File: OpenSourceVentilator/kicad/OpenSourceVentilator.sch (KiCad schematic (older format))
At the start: 7 parts, among them J101 Conn_TM1638_Disp, J102 12V Barrel Jack, J103 Conn_Stepper_Motor, U101 BME280

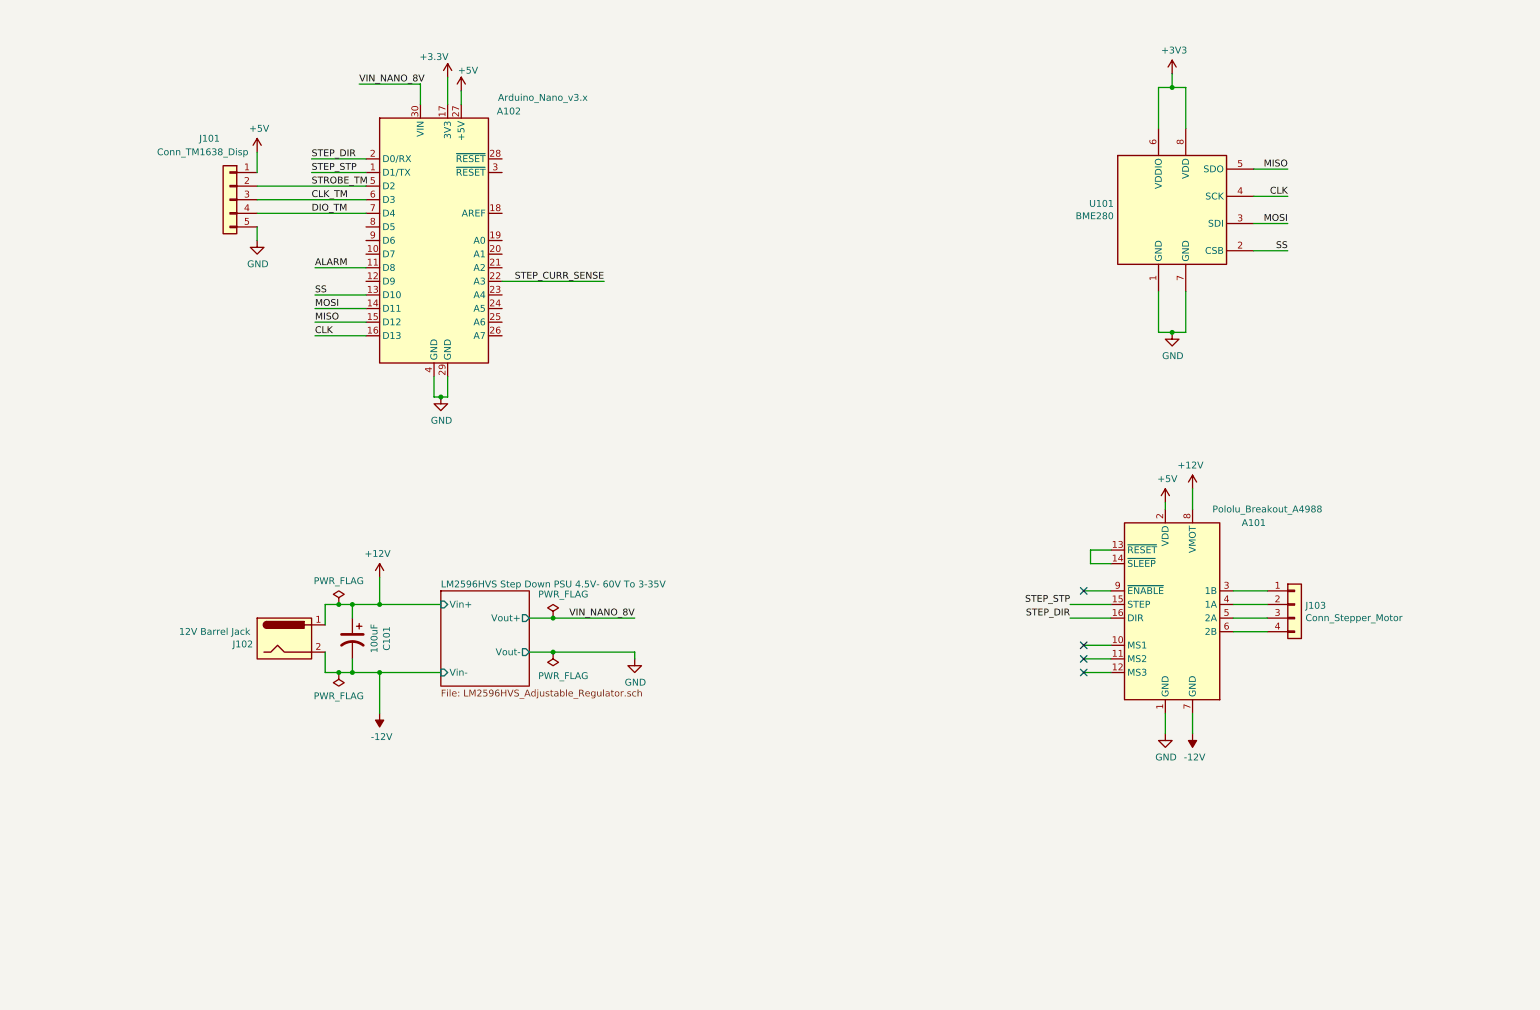
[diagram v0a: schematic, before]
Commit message: Initial schematic draft for OSV
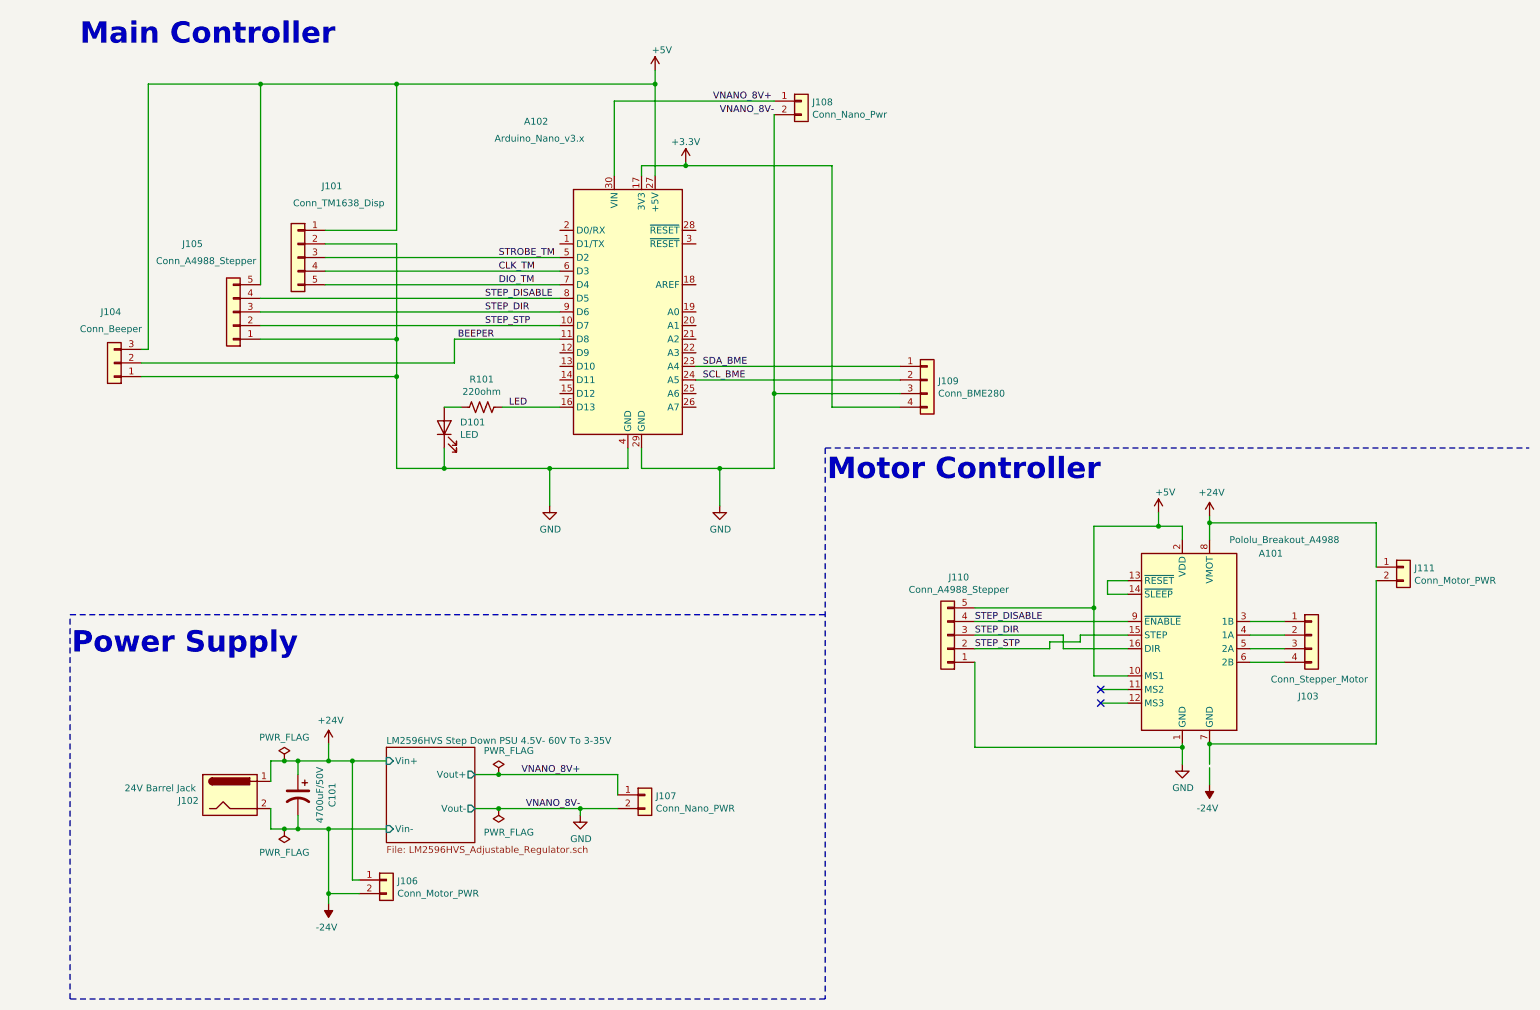
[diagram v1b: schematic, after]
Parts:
- removed U101: BME280, Package_LGA:Bosch_LGA-8_2.5x2.5mm_P0.65mm_ClockwisePinNumbering, symbol Sensor:BME280
- added D101: LED, symbol Device:LED
- added J104: Conn_Beeper, symbol Connector_Generic:Conn_01x03
- added J105, J110: Conn_A4988_Stepper, symbol Connector_Generic:Conn_01x05
- added J106, J111: Conn_Motor_PWR, symbol Connector_Generic:Conn_01x02
- added J107: Conn_Nano_PWR, symbol Connector_Generic:Conn_01x02
- added J108: Conn_Nano_Pwr, symbol Connector_Generic:Conn_01x02
- added J109: Conn_BME280, symbol Connector_Generic:Conn_01x04
- added R101: 220ohm, symbol Device:R_US
- C101: value 100uF -> 4700uF/50V
- J102: value 12V Barrel Jack -> 24V Barrel Jack
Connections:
- net +3V3: now also J109.4 (Pin_4)
- net +5V: now also A101.10 (MS1), J104.3 (Pin_3), J105.5 (Pin_5), J110.5 (Pin_5)
- net CLK_TM: now also J101.4 (Pin_4); no longer J101.3 (Pin_3)
- net DIO_TM: now also J101.5 (Pin_5); no longer J101.4 (Pin_4)
- net GND: now also J101.2 (Pin_2), D101.1 (K), J104.1 (Pin_1), J105.1 (Pin_1), J107.2 (Pin_2), J108.2 (Pin_2), J109.3 (Pin_3), J110.1 (Pin_1); no longer J101.5 (Pin_5)
- net STEP_DIR: now also A102.9 (D6), J105.3 (Pin_3), J110.3 (Pin_3); no longer A102.2 (D0/RX)
- net STEP_STP: now also A102.10 (D7), J105.2 (Pin_2), J110.2 (Pin_2); no longer A102.1 (D1/TX)
- net STROBE_TM: now also J101.3 (Pin_3); no longer J101.2 (Pin_2)
- net STEP_DISABLE: now reaches A101.9 (~ENABLE)
- net STEP_DISABLE: now also A102.8 (D5), J105.4 (Pin_4), J110.4 (Pin_4)
- net SDA_BME: now reaches A102.23 (A4)
- net SDA_BME: now also J109.1 (Pin_1)
- net SCL_BME: now reaches A102.24 (A5)
- net SCL_BME: now also J109.2 (Pin_2)
- net +12V renamed +24V
- net +24V: now also J106.1 (Pin_1), J111.1 (Pin_1)
- net -12V renamed -24V
- net -24V: now also J106.2 (Pin_2); no longer A101.7 (GND)
- net ALARM renamed BEEPER
- net BEEPER: now also J104.2 (Pin_2)
- net CLK renamed LED
- net LED: now also R101.2
- net MISO: no longer names the net of A102.15 (D12)
- net MOSI: no longer names the net of A102.14 (D11)
- net SS: no longer names the net of A102.13 (D10)
- net STEP_CURR_SENSE: no longer names the net of A102.22 (A3)
- net VIN_NANO_8V renamed VNANO_8V+
- net VNANO_8V+: now also J107.1 (Pin_1), J108.1 (Pin_1)
- new net: A101.7 (GND), J111.2 (Pin_2)
- new net: D101.2 (A), R101.1
- no-connect marks 4 -> 2
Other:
- note added: "Main Controller"
- note added: "Motor Controller"
- note added: "Power Supply"
- moved on the sheet: A101, A102, C101, J101, J102, J103
